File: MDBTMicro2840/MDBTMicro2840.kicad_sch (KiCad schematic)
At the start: 4 parts, among them J1 Conn_01x04, J2 USB_C_Receptacle_USB2.0, U1 MDBT50Q-x1MV2, U2 ProMicro

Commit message: Update sch
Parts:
- added C1, C2: 12pF, Capacitor_SMD:C_0201_0603Metric, symbol Device:C_Small
- added C3, C4: 10uF, Capacitor_SMD:C_0201_0603Metric, symbol Device:C_Small
- added D1: 1N5819, Diode_SMD:D_0201_0603Metric, symbol Diode:1N5819
- added LD1: RED, LED_SMD:LED_0201_0603Metric, symbol Device:LED
- added LD2: BLUE, LED_SMD:LED_0201_0603Metric, symbol Device:LED
- added R1, R5: 1k, Resistor_SMD:R_0201_0603Metric, symbol Device:R_Small_US
- added R2: Rprog, Resistor_SMD:R_0201_0603Metric, symbol Device:R_Small_US
- added R3: 820k, Resistor_SMD:R_0201_0603Metric, symbol Device:R_Small_US
- added R4: 2M, Resistor_SMD:R_0201_0603Metric, symbol Device:R_Small_US
- added R6, R7: 5.1k, Resistor_SMD:R_0201_0603Metric, symbol Device:R_Small_US
- added U3: XC6220B331MR-G, MDBTMicro_library:SOT-25-5, symbol MDBTMicro_library:XC6220B331MR-G
- added U4: TP4057, Package_TO_SOT_SMD:SOT-23-6, symbol MDBTMicro_library:TP4057
- added Y1: 32.768kHz, Crystal:Crystal_SMD_3215-2Pin_3.2x1.5mm, symbol Device:Crystal
- J1: value Conn_01x04 -> SWD
- J2: footprint Connector_USB:USB_C_Receptacle_Palconn_UTC16-G -> Connector_USB:USB_C_Receptacle_HRO_TYPE-C-31-M-12
- U1: footprint MDBTMicro_library:MDBT50Q -> RF_Module:Raytac_MDBT50Q
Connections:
- net VDD is gone; now on net nRF_VDD: J1.1 (Pin_1), U1.28 (VDD)
- net GND: now also U1.15 (GND), U1.33 (GND), U1.55 (GND), U2.14 (GND), C1.1, C2.1, C3.1, C4.1, R2.1, R4.1, R5.1, R6.2, R7.2, U3.2 (VSS), U4.2 (GND); no longer J2.S1 (SHIELD)
- net VBUS: now also C3.2, D1.1 (K), R1.2, U3.1 (VIN), U3.3 (CE), U4.4 (VCC)
- net VBAT: now reaches U2.13 (RAW)
- net VBAT: now also D1.2 (A), R3.2, U4.3 (BAT)
- net nRF_VDD: now reaches U2.16 (VCC)
- net nRF_VDD: now also U1.30 (VDDH), C4.2, U3.5 (VOUT)
- net at J2.A5 (CC1): now also R6.1
- net at J2.B5 (CC2): now also R7.1
- net at U1.17 (P0.00/XL1): now also C1.2, Y1.2
- net at U1.18 (P0.01/XL2): now also C2.2, Y1.1
- net BATTERT_PIN: now reaches U1.20 (P0.04/AIN2)
- net BATTERT_PIN: now also R3.1, R4.2
- net LED_PIN: now reaches U1.3 (P1.10)
- net LED_PIN: now also LD2.2 (A)
- net SWDCLK renamed SWCLK
- new net: R2.2, U4. (PROG6)
- new net: LD1.1 (K), U4.1 (CHRG)
- new net: LD2.1 (K), R5.2
- new net: LD1.2 (A), R1.1
- no-connect marks 2 -> 5
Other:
- note added: "LiPo Charging"
- note added: "Power"
- note added: "Rprog(ohm) Ibat(mA) 20k 50 10k 100 5k 200 4k 250 3k 300 2k 400 1.6k 500"
- moved on the sheet: J1, J2

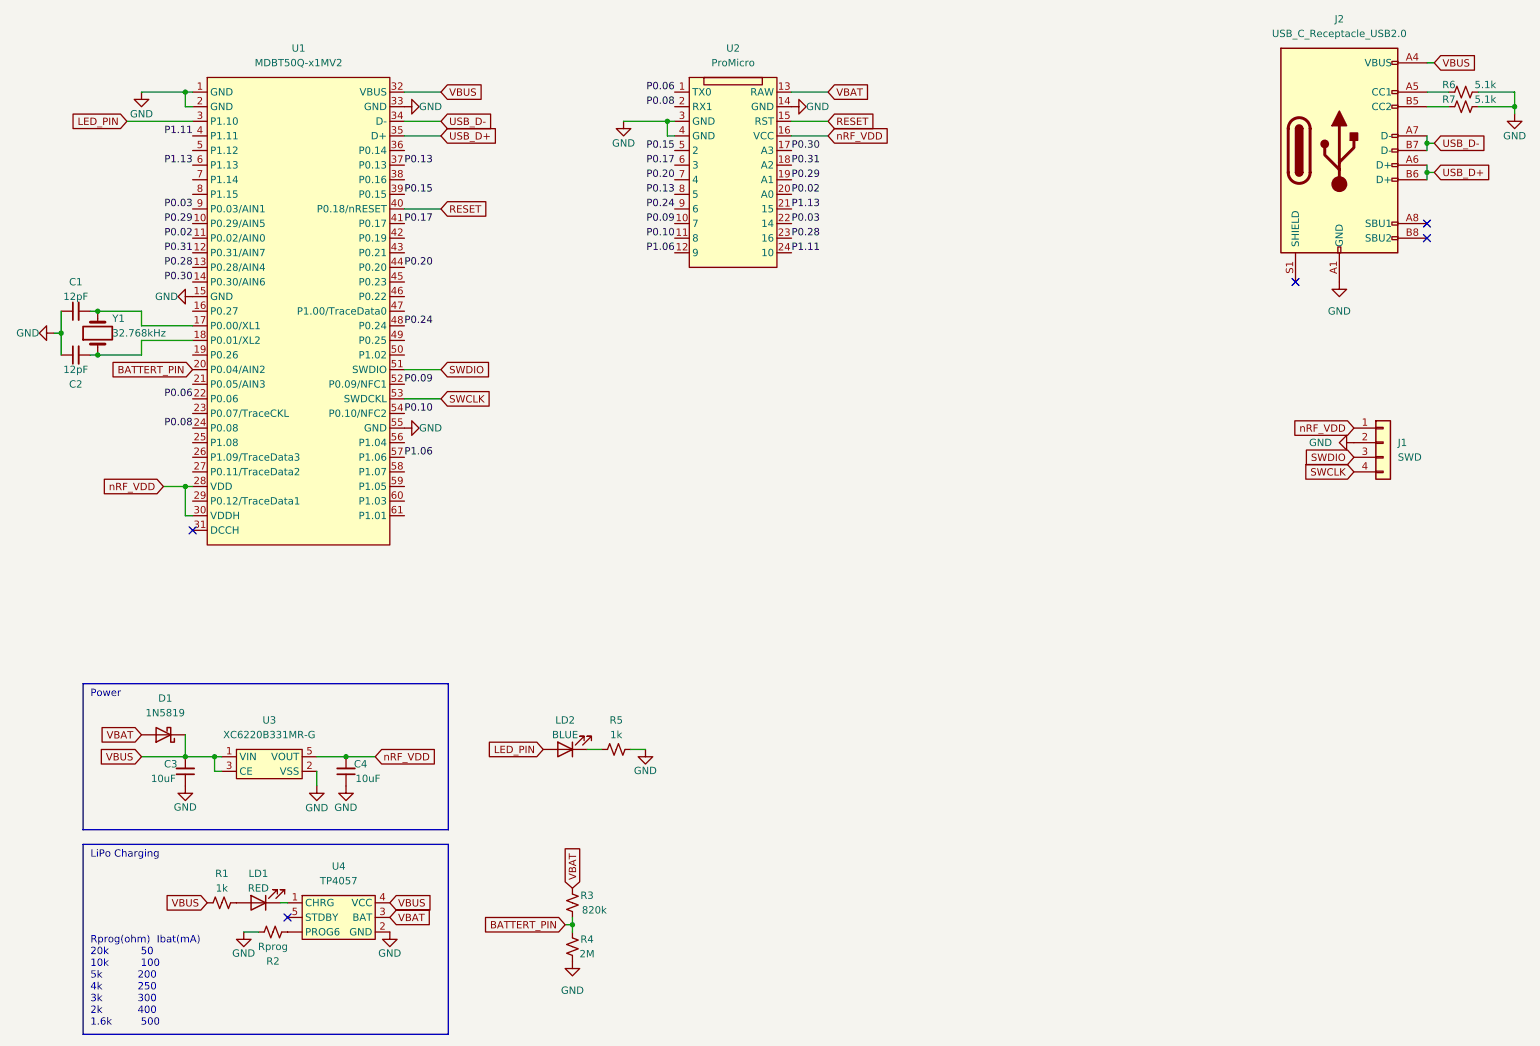
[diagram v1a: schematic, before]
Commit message: Update USB footprint
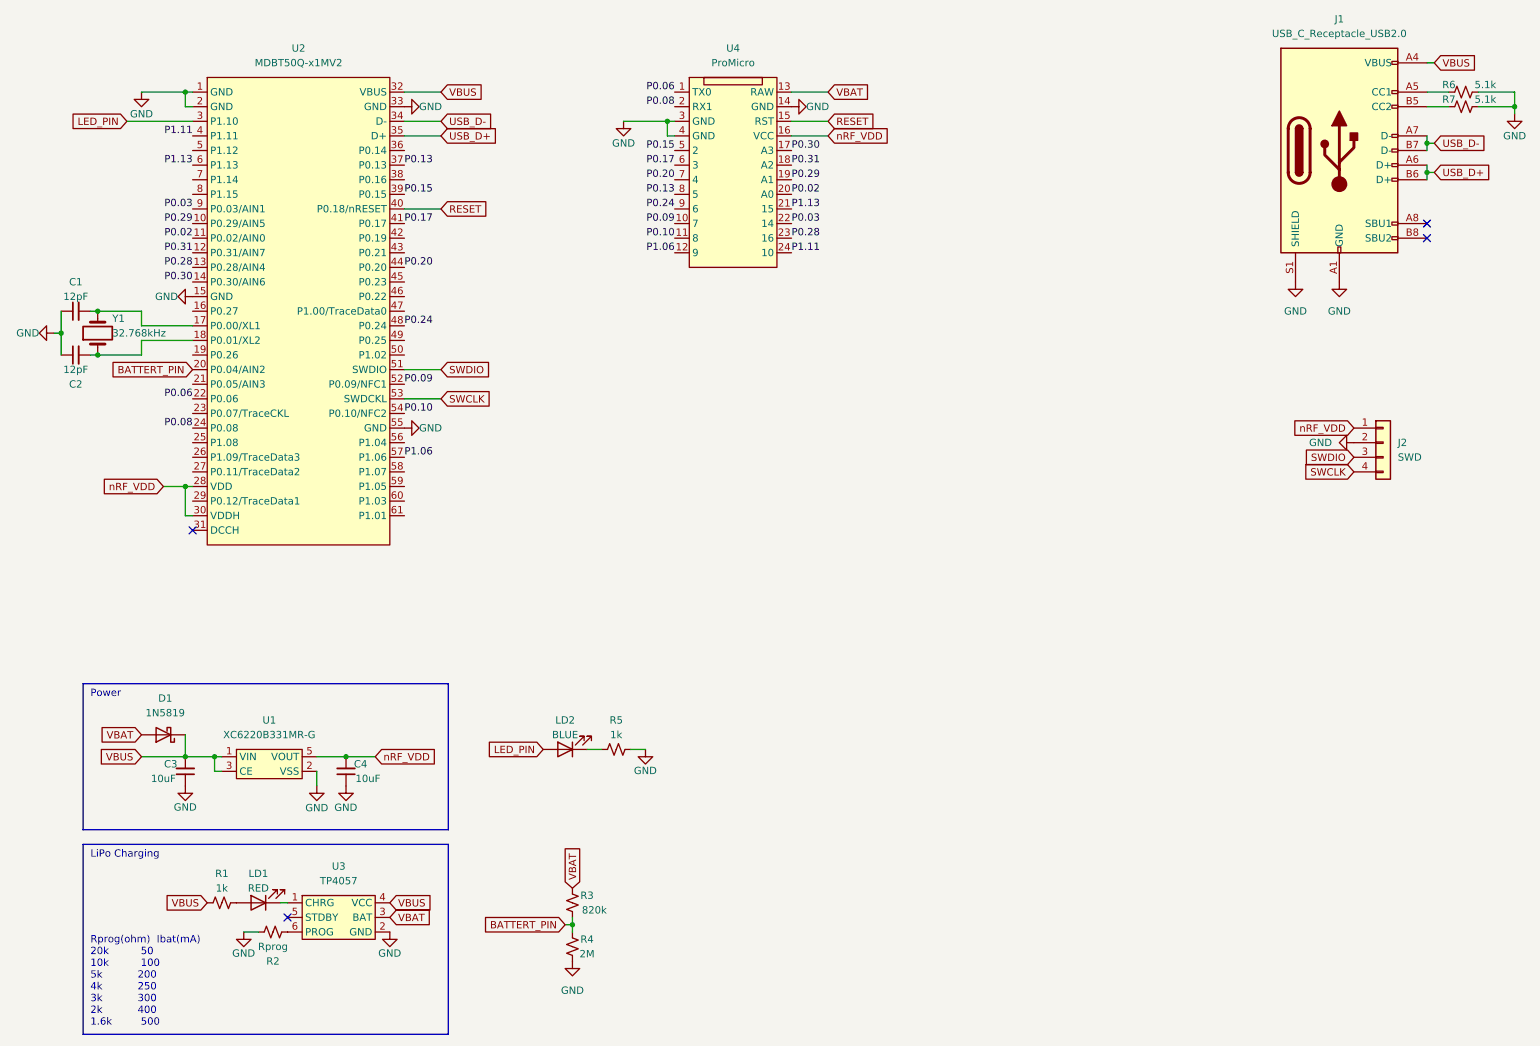
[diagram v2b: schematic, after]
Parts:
- J1: renamed from J2; footprint Connector_USB:USB_C_Receptacle_HRO_TYPE-C-31-M-12 -> MDBTMicro_library:USB Type-C Mid-Mount Receptacle 16P
- renumbered J1 to J2, U3 to U1, U1 to U2, U4 to U3, U2 to U4
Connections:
- net GND: now also J1.S1 (SHIELD)
- net at R2.2: now also U3.6 (PROG); no longer U3. (PROG6)
- no-connect marks 5 -> 4
